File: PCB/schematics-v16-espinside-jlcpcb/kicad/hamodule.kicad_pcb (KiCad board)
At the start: 2 copper layers, 76.7 x 84.3 mm, 81 parts, among them J1 2604-1104, J10 EspSense, J11 Conn_01x02_Male, J2 2604-1102, J3 USB_B_Micro, J4 ESP Relays, J5 Current Jumper, J6 GND 3.3V, J7 Conn_01x02, J8 Current Jumper, J9 2604-1104, K1 PCN-105D, K2 PCN-105D, K3 PCN-105D, K4 PCN-105D, Q1 SS8050, Q2 SS8050, SW1 EN, SW2 IO0, U1 ULN2003A, U2 ESP32-WROOM-32D, U4 LD1117AV33_TO220, U5 MCP9700T-ETT, U6 LDA210-PDIP, U7 LDA210-PDIP, U8 CP2102N-A01-GQFN28

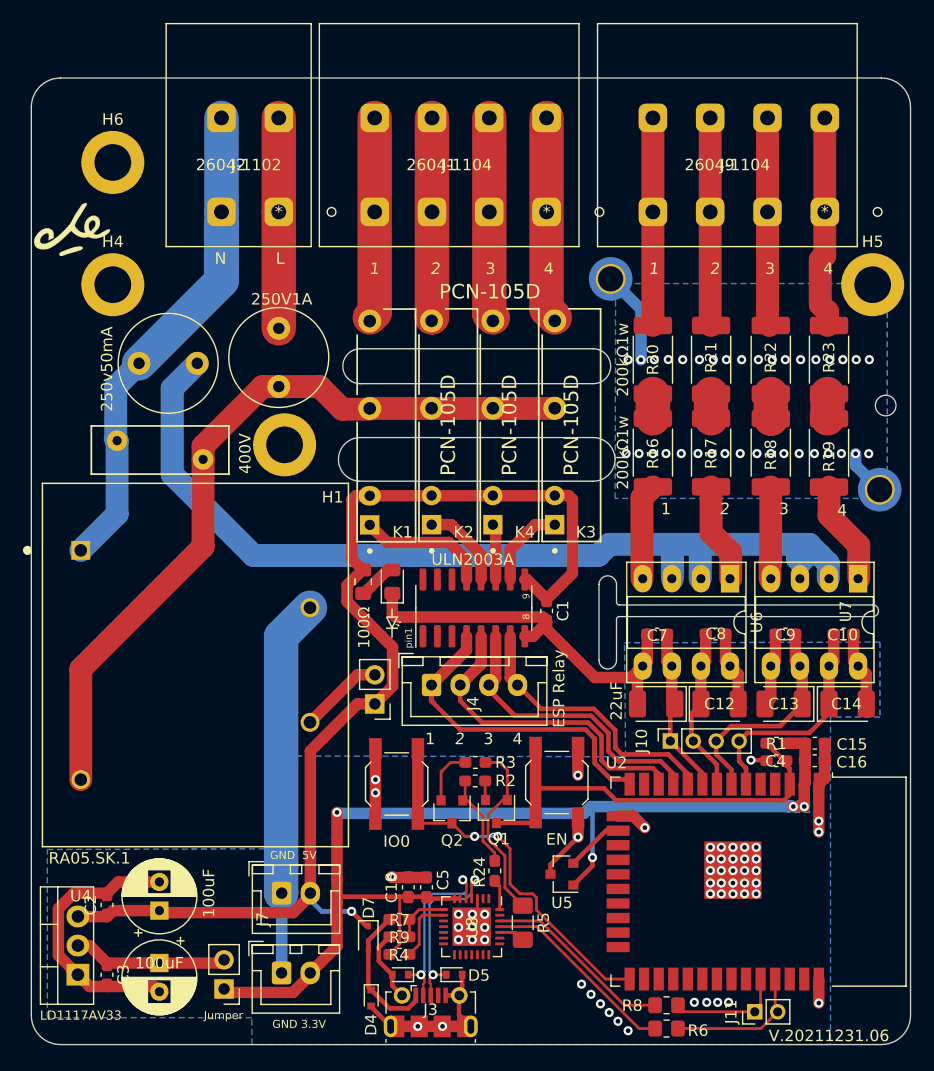
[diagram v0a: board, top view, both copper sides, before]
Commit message: changed big caps + readme + routing + JLCPCB
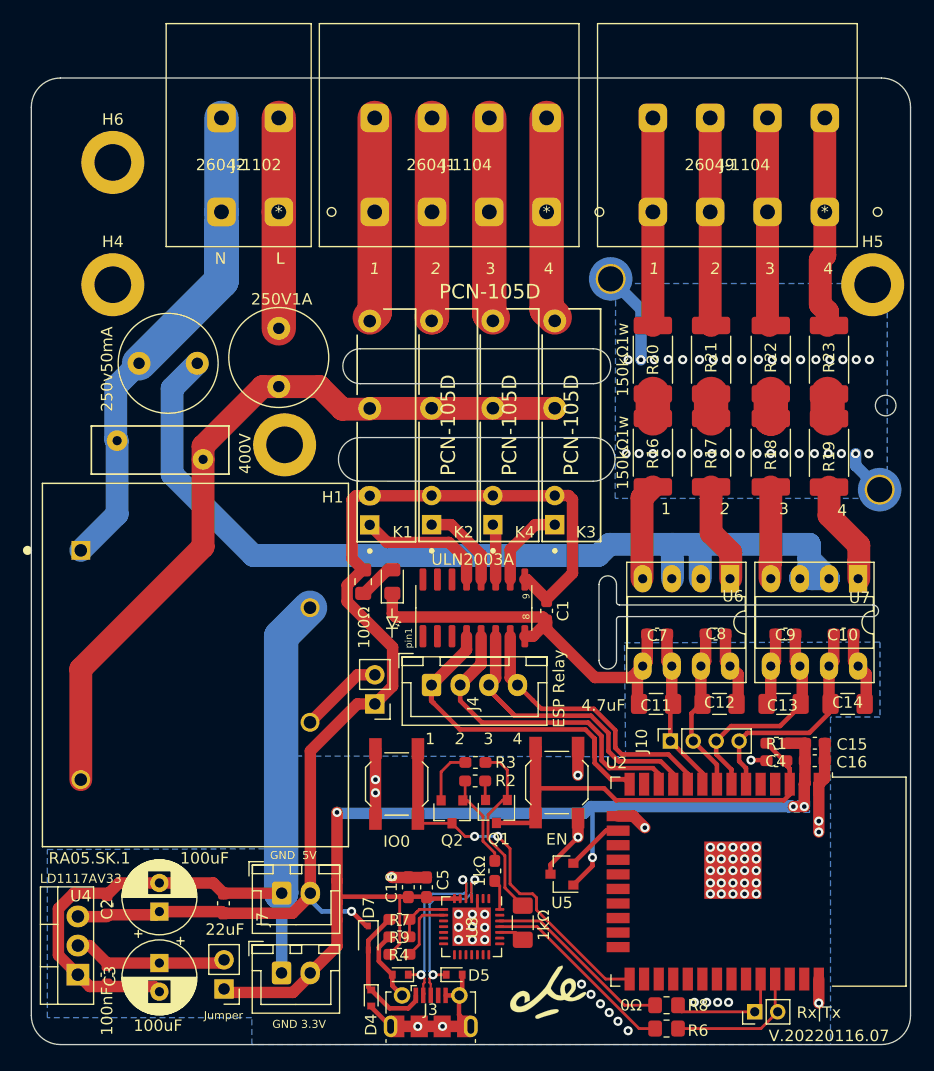
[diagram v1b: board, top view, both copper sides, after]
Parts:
- added C6: 22uF, Capacitor_SMD:C_0603_1608Metric_Pad1.08x0.95mm_HandSolder, F.Cu at (141.9, 139.4)
- C11, C12, C13, C14: value 22uF -> 4.7uF; footprint Capacitor_Tantalum_SMD:CP_EIA-3528-21_Kemet-B_Pad1.50x2.35mm_HandSolder -> Capacitor_SMD:C_1206_3216Metric_Pad1.42x1.75mm_HandSolder
- R16, R17, R18, R19, R20, R21, R22, R23: value 200kΩ1w -> 150kΩ1w
- U2: value ESP32-WROOM-32D -> ESP32-WROOM-32E
- moved G*** 78.4 mm to (170.2, 147.1)
- moved 100uF_1 0.09 mm to (136.3, 140.1)
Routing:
- net GND: track 195.4 -> 206.5 mm
- net 220VAC(N): track 82.7 -> 87.1 mm
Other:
- board text added: "V.20220116.07"
- board text removed: "V.20211231.06"
